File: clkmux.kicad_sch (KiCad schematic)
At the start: 9 parts, among them J7 Conn_Coaxial, U3 9DMV0141AKILF, U4 DS90C401M_NOPB

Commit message: add a footprint for QPix ASIC CoB  and its generator
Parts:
- J7: footprint Connector_Coaxial:BNC_TEConnectivity_1478035_Horizontal -> Connector_Coaxial:SMA_Amphenol_901-144_Vertical
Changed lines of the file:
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@@
     (property "Reference" "J7" (id 0) (at 60.0074 72.39 0))
     (property "Value" "Conn_Coaxial" (id 1) (at 60.0074 74.93 0))
-    (property "Footprint" "Connector_Coaxial:BNC_TEConnectivity_1478035_Horizontal" (id 2) (at 59.69 80.01 0)
+    (property "Footprint" "Connector_Coaxial:SMA_Amphenol_901-144_Vertical" (id 2) (at 59.69 80.01 0)
       (effects (font (size 1.27 1.27)) hide)
     )

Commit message: some progress in routing
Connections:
- net SEL_AB: now reaches JP1.1 (A), R13.1, U3.14 (^SEL_A_B#)
- net DO-: now reaches U3.16 (DIF_INA#), U4.6 (DO2-)
- net DO+: now reaches U3.15 (DIF_INA), U4.7 (DO2+)
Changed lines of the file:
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@@
     (stroke (width 0) (type default) (color 0 0 0 0))
+  )
+  (label "DO-" (at 120.65 77.47 0)
+    (effects (font (size 1.27 1.27)) (justify left bottom))
+  )
+  (label "SEL_AB" (at 146.05 76.2 0)
+    (effects (font (size 1.27 1.27)) (justify left bottom))
+  )
+  (label "DO+" (at 120.65 74.93 0)
+    (effects (font (size 1.27 1.27)) (justify left bottom))
   )
   (global_label "CLKOUTP" (shape output) (at 135.89 139.7 270) (fields_autoplaced)

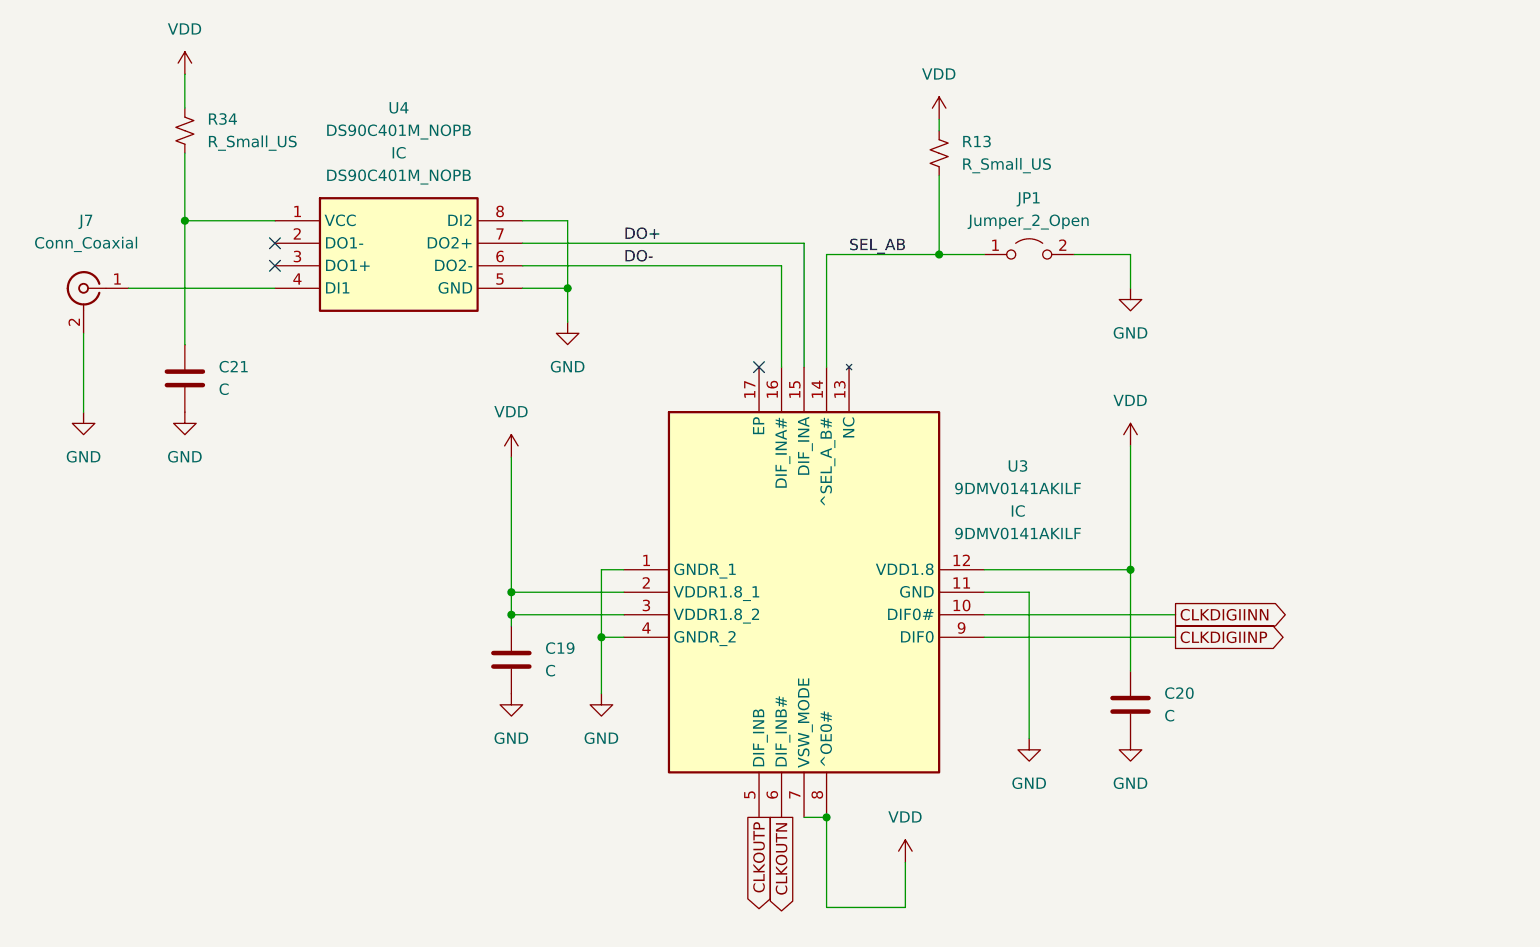
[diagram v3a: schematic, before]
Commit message: add part values for missed ones
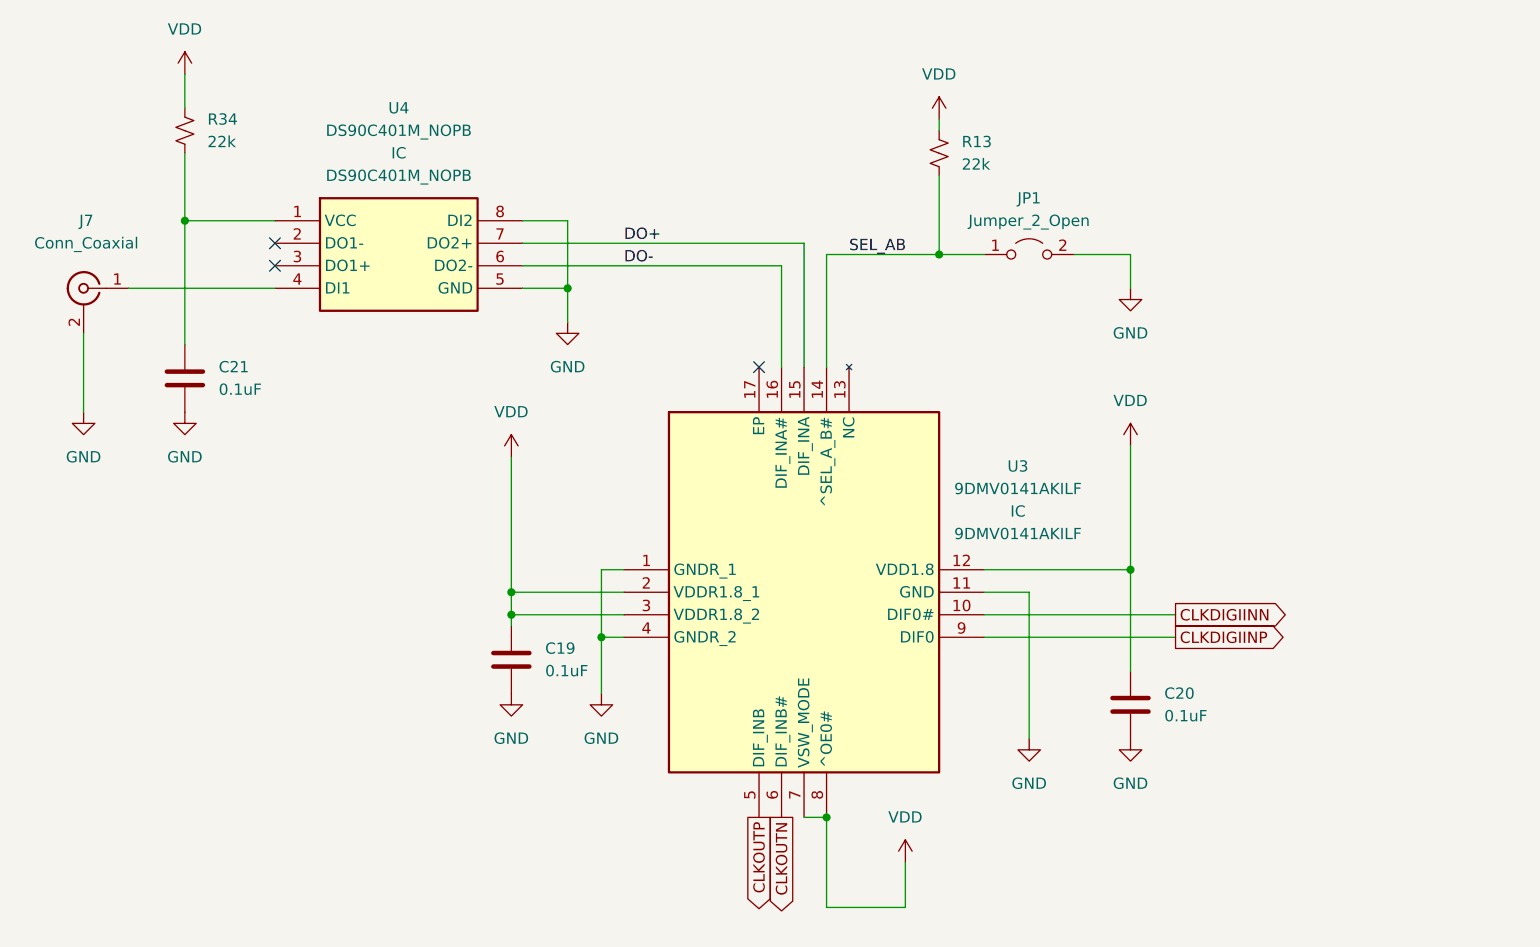
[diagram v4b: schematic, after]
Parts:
- C19, C20, C21: value C -> 0.1uF
- R13, R34: value R_Small_US -> 22k
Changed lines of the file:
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@@
   (symbol (lib_id "Device:C") (at 107.95 121.92 0) (unit 1)
     (in_bom yes) (on_board yes) (dnp no) (fields_autoplaced)
-    (property "Reference" "C19" (at 111.76 120.6499 0)
-      (effects (font (size 1.27 1.27)) (justify left))
-    )
-    (property "Value" "C" (at 111.76 123.1899 0)
+    (property "Reference" "C19" (at 111.76 120.65 0)
+      (effects (font (size 1.27 1.27)) (justify left))
+    )
+    (property "Value" "0.1uF" (at 111.76 123.19 0)
       (effects (font (size 1.27 1.27)) (justify left))
     )
@@
   (symbol (lib_id "Device:C") (at 71.12 90.17 0) (unit 1)
     (in_bom yes) (on_board yes) (dnp no) (fields_autoplaced)
-    (property "Reference" "C21" (at 74.93 88.8999 0)
-      (effects (font (size 1.27 1.27)) (justify left))
-    )
-    (property "Value" "C" (at 74.93 91.4399 0)
+    (property "Reference" "C21" (at 74.93 88.9 0)
+      (effects (font (size 1.27 1.27)) (justify left))
+    )
+    (property "Value" "0.1uF" (at 74.93 91.44 0)
       (effects (font (size 1.27 1.27)) (justify left))
     )
@@
       (effects (font (size 1.27 1.27)) (justify right))
     )
-    (property "Value" "R_Small_US" (at 158.75 66.0399 0)
+    (property "Value" "22k" (at 158.75 66.0399 0)
       (effects (font (size 1.27 1.27)) (justify right))
     )
@@
       (effects (font (size 1.27 1.27)) (justify left))
     )
-    (property "Value" "C" (at 181.61 128.2699 0)
+    (property "Value" "0.1uF" (at 181.61 128.2699 0)
       (effects (font (size 1.27 1.27)) (justify left))
     )
@@
       (effects (font (size 1.27 1.27)) (justify right))
     )
-    (property "Value" "R_Small_US" (at 73.66 63.4999 0)
+    (property "Value" "22k" (at 73.66 63.4999 0)
       (effects (font (size 1.27 1.27)) (justify right))
     )

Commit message: fix external clock input
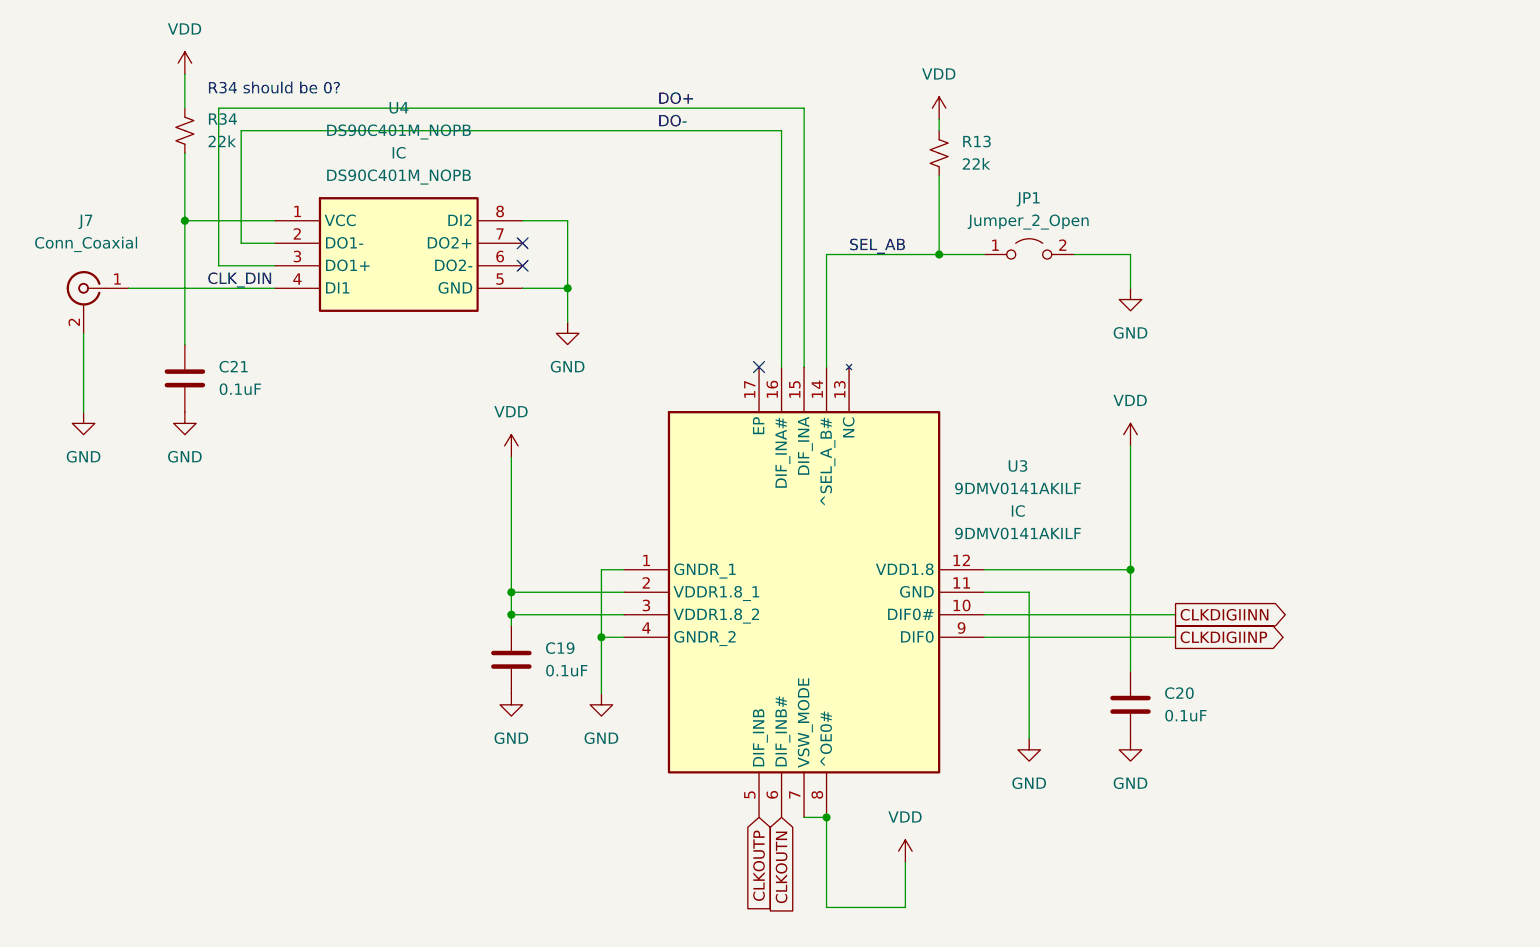
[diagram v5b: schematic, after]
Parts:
- U4: footprint 9DMV0141AKILF:QFN50P300X300X100-17N -> DS90C401M:SOIC127P600X175-8N
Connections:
- net DO+: now also U4.3 (DO1+); no longer U4.7 (DO2+)
- net DO-: now also U4.2 (DO1-); no longer U4.6 (DO2-)
- net CLK_DIN: now reaches J7.1 (In), U4.4 (DI1)
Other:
- note added: "R34 should be 0?"
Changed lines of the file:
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@@
   (junction (at 107.95 114.3) (diameter 0) (color 0 0 0 0)
   )
-  (no_connect (at 81.28 74.93))
+  (no_connect (at 109.22 77.47))
   (no_connect (at 135.89 88.9))
-  (no_connect (at 81.28 77.47))
+  (no_connect (at 109.22 74.93))
+  (wire (pts (xy 77.47 74.93) (xy 77.47 62.23))
+    (stroke (width 0) (type default))
+  )
   (wire (pts (xy 140.97 139.7) (xy 143.51 139.7))
     (stroke (width 0) (type default))
@@
     (stroke (width 0) (type default))
   )
+  (wire (pts (xy 74.93 77.47) (xy 74.93 59.69))
+    (stroke (width 0) (type default))
+  )
   (wire (pts (xy 64.77 80.01) (xy 81.28 80.01))
     (stroke (width 0) (type default))
   )
-  (wire (pts (xy 109.22 77.47) (xy 138.43 77.47))
-    (stroke (width 0) (type default))
-  )
   (wire (pts (xy 120.65 116.84) (xy 107.95 116.84))
     (stroke (width 0) (type default))
@@
     (stroke (width 0) (type default))
   )
-  (wire (pts (xy 138.43 77.47) (xy 138.43 88.9))
-    (stroke (width 0) (type default))
-  )
   (wire (pts (xy 114.3 72.39) (xy 114.3 80.01))
     (stroke (width 0) (type default))
@@
     (stroke (width 0) (type default))
   )
+  (wire (pts (xy 74.93 59.69) (xy 140.97 59.69))
+    (stroke (width 0) (type default))
+  )
   (wire (pts (xy 156.21 76.2) (xy 161.29 76.2))
     (stroke (width 0) (type default))
@@
     (stroke (width 0) (type default))
   )
-  (wire (pts (xy 109.22 74.93) (xy 140.97 74.93))
+  (wire (pts (xy 138.43 62.23) (xy 138.43 88.9))
     (stroke (width 0) (type default))
   )
@@
     (stroke (width 0) (type default))
   )
+  (wire (pts (xy 74.93 77.47) (xy 81.28 77.47))
+    (stroke (width 0) (type default))
+  )
   (wire (pts (xy 182.88 119.38) (xy 161.29 119.38))
     (stroke (width 0) (type default))
@@
     (stroke (width 0) (type default))
   )
+  (wire (pts (xy 140.97 59.69) (xy 140.97 88.9))
+    (stroke (width 0) (type default))
+  )
   (wire (pts (xy 118.11 111.76) (xy 118.11 119.38))
     (stroke (width 0) (type default))
   )
-  (wire (pts (xy 140.97 74.93) (xy 140.97 88.9))
+  (wire (pts (xy 77.47 62.23) (xy 138.43 62.23))
     (stroke (width 0) (type default))
   )
@@
     (stroke (width 0) (type default))
   )
+  (wire (pts (xy 81.28 74.93) (xy 77.47 74.93))
+    (stroke (width 0) (type default))
+  )
   (wire (pts (xy 107.95 99.06) (xy 107.95 114.3))
     (stroke (width 0) (type default))
@@
     (stroke (width 0) (type default))
   )
-  (label "DO-" (at 120.65 77.47 0) (fields_autoplaced)
+  (text "R34 should be 0?" (at 73.66 58.42 0)
+    (effects (font (size 1.27 1.27)) (justify left bottom))
+  )
+  (label "DO-" (at 124.46 62.23 0) (fields_autoplaced)
     (effects (font (size 1.27 1.27)) (justify left bottom))
   )
@@
     (effects (font (size 1.27 1.27)) (justify left bottom))
   )
-  (label "DO+" (at 120.65 74.93 0) (fields_autoplaced)
+  (label "DO+" (at 124.46 59.69 0) (fields_autoplaced)
     (effects (font (size 1.27 1.27)) (justify left bottom))
   )
-  (global_label "CLKOUTP" (shape output) (at 135.89 139.7 270) (fields_autoplaced)
+  (label "CLK_DIN" (at 73.66 80.01 0) (fields_autoplaced)
+    (effects (font (size 1.27 1.27)) (justify left bottom))
+  )
+  (global_label "CLKOUTP" (shape input) (at 135.89 139.7 270) (fields_autoplaced)
     (effects (font (size 1.27 1.27)) (justify right))
-    (property "Intersheetrefs" "${INTERSHEET_REFS}" (at 135.9694 150.5798 90)
+    (property "Intersheetrefs" "${INTERSHEET_REFS}" (at 135.89 151.1519 90)
       (effects (font (size 1.27 1.27)) (justify right) hide)
     )
@@
     )
   )
-  (global_label "CLKOUTN" (shape output) (at 138.43 139.7 270) (fields_autoplaced)
+  (global_label "CLKOUTN" (shape input) (at 138.43 139.7 270) (fields_autoplaced)
     (effects (font (size 1.27 1.27)) (justify right))
-    (property "Intersheetrefs" "${INTERSHEET_REFS}" (at 138.5094 150.6402 90)
+    (property "Intersheetrefs" "${INTERSHEET_REFS}" (at 138.43 151.2124 90)
       (effects (font (size 1.27 1.27)) (justify right) hide)
     )
@@
       (effects (font (size 1.27 1.27)))
     )
-    (property "Footprint" "9DMV0141AKILF:QFN50P300X300X100-17N" (at 81.28 72.39 0)
-      (effects (font (size 1.27 1.27)) hide)
-    )
+    (property "Footprint" "DS90C401M:SOIC127P600X175-8N" (at 81.28 72.39 0)
+      (effects (font (size 1.27 1.27)) hide)
+    )
